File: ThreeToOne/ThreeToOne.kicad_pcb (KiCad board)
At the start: 2 copper layers, 216 parts, among them SW1 Switch, SW10 Switch, SW100 Switch, SW101 Switch, SW11 Switch, SW12 Switch, SW13 Switch, SW14 Switch, SW15 Switch, SW16 Switch, SW17 REsw, SW18 Switch, SW19 Switch, SW2 Switch, SW20 Switch, SW21 Switch, SW22 Switch, SW23 Switch, SW24 Switch, SW25 Switch, SW26 Switch, SW27 Switch, SW28 Switch, SW29 Switch, SW3 Switch, SW30 Switch, SW31 Switch, SW32 Switch, SW33 Switch, SW34 Switch, SW35 Switch, SW36 Switch, SW37 Switch, SW38 Switch, SW39 Switch, SW4 Switch, SW40 Switch, SW41 Switch, SW42 Switch, SW43 Switch, SW44 Switch, SW45 Switch, SW46 Switch, SW47 Switch, SW48 Switch, SW49 Switch, SW5 Switch, SW50 Switch, SW51 Switch, SW52 Switch, SW53 Switch, SW54 Switch, SW55 Switch, SW56 Switch, SW57 Switch, SW58 Switch, SW59 Switch, SW6 Switch, SW60 Switch, SW61 Switch, SW62 Switch, SW63 Switch, SW64 Switch, SW65 Switch, SW66 Switch, SW67 Switch, SW68 Switch, SW69 Switch, SW7 Switch, SW70 Switch, SW71 Switch, SW72 Switch, SW73 Switch, SW74 Switch, SW75 Switch, SW76 Switch, SW77 Switch, SW78 Switch, SW79 Switch, SW8 Switch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

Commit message: Laid out and routed rows/cols
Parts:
- removed H1, H10, H11, H12, H2, H3, H4, H5, H6, H7, H8, H9: Hole, KeyboardFootprints:Hole_2mm
- moved U2 457.7 mm to (464.3, 131.8)
- moved U1 81.4 mm to (302.4, 131.8)
- moved D75 18.7 mm to (303.2, 231.0)
- moved D52 0.79 mm to (521.5, 197.6)
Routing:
- net Row5: track 0.00 -> 331.6 mm
- net Col8: track 0.00 -> 180.6 mm
- net Col0: track 0.00 -> 180.3 mm
- net Col4: track 0.00 -> 179.6 mm
- net Row4: track 0.00 -> 176.8 mm
- net Col2: track 0.00 -> 175.2 mm
- net Row0: track 0.00 -> 174.6 mm
- net Row3: track 0.00 -> 174.6 mm
- net Row1: track 0.00 -> 174.6 mm
- net Row7: track 0.00 -> 174.6 mm
- net Row2: track 0.00 -> 174.6 mm
- net Col1: track 0.00 -> 174.6 mm
- net Col7: track 0.00 -> 173.0 mm
- net Col9: track 0.00 -> 171.7 mm
- net Col10: track 0.00 -> 171.6 mm
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
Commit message: Wired all of left half and some of right
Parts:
- added H1: Hole, KeyboardFootprints:Hole_2mm, F.Cu at (231.9, 75.5)
- added H10: Hole, KeyboardFootprints:Hole_2mm, F.Cu at (237.9, 81.5)
- added H11: Hole, KeyboardFootprints:Hole_2mm, F.Cu at (240.9, 78.5)
- added H12: Hole, KeyboardFootprints:Hole_2mm, F.Cu at (243.9, 75.5)
- added H2: Hole, KeyboardFootprints:Hole_2mm, F.Cu at (231.9, 78.5)
- added H3: Hole, KeyboardFootprints:Hole_2mm, F.Cu at (234.9, 75.5)
- added H4: Hole, KeyboardFootprints:Hole_2mm, F.Cu at (231.9, 81.5)
- added H5: Hole, KeyboardFootprints:Hole_2mm, F.Cu at (234.9, 78.5)
- added H6: Hole, KeyboardFootprints:Hole_2mm, F.Cu at (237.9, 75.5)
- added H7: Hole, KeyboardFootprints:Hole_2mm, F.Cu at (234.9, 81.5)
- added H8: Hole, KeyboardFootprints:Hole_2mm, F.Cu at (237.9, 78.5)
- added H9: Hole, KeyboardFootprints:Hole_2mm, F.Cu at (240.9, 75.5)
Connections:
- SW17 pad A: (no net) -> E3
- SW17 pad B: (no net) -> E4
- SW17 pad C: (no net) -> E2GND
- SW91 pad A: (no net) -> E1
- SW91 pad B: (no net) -> E2
- SW91 pad C: (no net) -> EGND1
- U1 pad 1: (no net) -> Col8
- U1 pad 10: (no net) -> Col4
- U1 pad 11: (no net) -> Col3
- U1 pad 12: (no net) -> Col2
- U1 pad 13: (no net) -> Row5
- U1 pad 14: (no net) -> Row4
- U1 pad 15: (no net) -> Row3
- U1 pad 16: (no net) -> Row2
- U1 pad 17: (no net) -> Row1
- U1 pad 18: (no net) -> Row0
- U1 pad 19: (no net) -> Col0
- U1 pad 2: (no net) -> Col7
- U1 pad 20: (no net) -> Col1
- U1 pad 21: (no net) -> TRRSVcc
- U1 pad 23: (no net) -> EGND1
- U1 pad 4: (no net) -> TRRSGnd
- U1 pad 5: (no net) -> Col6
- U1 pad 7: (no net) -> E2
- U1 pad 8: (no net) -> E1
- U1 pad 9: (no net) -> Col5
- U2 pad 1: (no net) -> Col9
- U2 pad 10: (no net) -> Col15
- U2 pad 11: (no net) -> Col16
- U2 pad 12: (no net) -> Col17
- U2 pad 13: (no net) -> E3
- U2 pad 14: (no net) -> E4
- U2 pad 15: (no net) -> Row11
- U2 pad 16: (no net) -> Row10
- U2 pad 17: (no net) -> Row9
- U2 pad 18: (no net) -> Row8
- U2 pad 19: (no net) -> Row7
- U2 pad 2: (no net) -> Col10
- U2 pad 20: (no net) -> Row6
- U2 pad 21: TRRSComm -> TRRSVcc
- U2 pad 23: (no net) -> E2GND
- U2 pad 3: TRRSComm -> (no net)
- U2 pad 4: (no net) -> TRRSGnd
- U2 pad 5: (no net) -> Col11
- U2 pad 7: (no net) -> Col12
- U2 pad 8: (no net) -> Col13
- U2 pad 9: (no net) -> Col14
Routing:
- net TRRSVcc: track 0.00 -> 162.6 mm, vias 0 -> 1
- net Row4: track 176.8 -> 339.0 mm, vias 0 -> 1
- net TRRSComm: track 0.00 -> 151.8 mm
- net Row3: track 174.6 -> 319.9 mm, vias 0 -> 1
- net E2: track 0.00 -> 144.3 mm, vias 0 -> 1
- net TRRSGnd: track 0.00 -> 140.5 mm
- net E1: track 0.00 -> 136.6 mm, vias 0 -> 1
- net Row2: track 174.6 -> 303.6 mm, vias 0 -> 1
- net EGND1: track 0.00 -> 115.6 mm, vias 0 -> 4
- net Row1: track 174.6 -> 286.6 mm, vias 0 -> 1
- net Row0: track 174.6 -> 269.3 mm, vias 0 -> 1
- net Col0: track 180.3 -> 273.5 mm
- net Col2: track 175.2 -> 266.9 mm
- net Col1: track 174.6 -> 252.5 mm
- net Col3: track 141.9 -> 217.9 mm
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
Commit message: Finished + gerbers
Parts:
- removed H1, H10, H11, H12, H2, H3, H4, H5, H6, H7, H8, H9: Hole, KeyboardFootprints:Hole_2mm
- added LED0: Diode, KeyboardFootprints:Diode, F.Cu at (461.2, 151.0)
- added LED1: Diode, KeyboardFootprints:Diode, F.Cu at (467.5, 150.8)
- added R0: Resistor, KeyboardFootprints:Resistor, F.Cu at (458.0, 151.0)
- added R1: Resistor, KeyboardFootprints:Resistor, F.Cu at (470.7, 150.8)
- U2: value ProMicro -> Elite-C; footprint KeyboardFootprints:ProMicro -> Keebio-Parts:Elite-C
- moved D89 18.3 mm to (264.3, 249.9)
- moved D87 17.5 mm to (225.4, 250.0)
- moved D88 17.5 mm to (244.5, 250.0)
- moved U1 9.52 mm to (292.9, 131.8)
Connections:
- U2 pad 13: E3 -> Net-(LED1-Pad1)
- U2 pad 14: E4 -> Net-(LED0-Pad1)
- U2 pad 15: Row11 -> Row8
- U2 pad 16: Row10 -> Row9
- U2 pad 17: Row9 -> Row10
- U2 pad 18: Row8 -> Row11
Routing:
- net Row11: track 160.9 -> 317.5 mm, vias 0 -> 1
- net E2GND: track 0.00 -> 147.8 mm, vias 0 -> 1
- net Row10: track 150.9 -> 295.7 mm, vias 0 -> 1
- net Row9: track 166.6 -> 294.4 mm, vias 0 -> 1
- net E4: track 0.00 -> 84.9 mm
- net E3: track 0.00 -> 76.8 mm, vias 0 -> 1
- net Row7: track 174.6 -> 247.4 mm, vias 0 -> 2
- net Row6: track 167.1 -> 223.8 mm
- net Net-(LED0-Pad1): track 0.00 -> 32.9 mm, vias 0 -> 1
- net Net-(LED1-Pad1): track 0.00 -> 29.5 mm, vias 0 -> 1
- net TRRSGnd: track 140.5 -> 168.8 mm, vias 0 -> 2
- net Row5: track 333.3 -> 306.0 mm
- net Row8: track 202.8 -> 229.0 mm, vias 0 -> 1
- net TRRSComm: track 151.8 -> 177.9 mm, vias 0 -> 2
- net Col13: track 165.1 -> 179.7 mm, vias 0 -> 2
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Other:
- board outline added: 343 x 133 mm

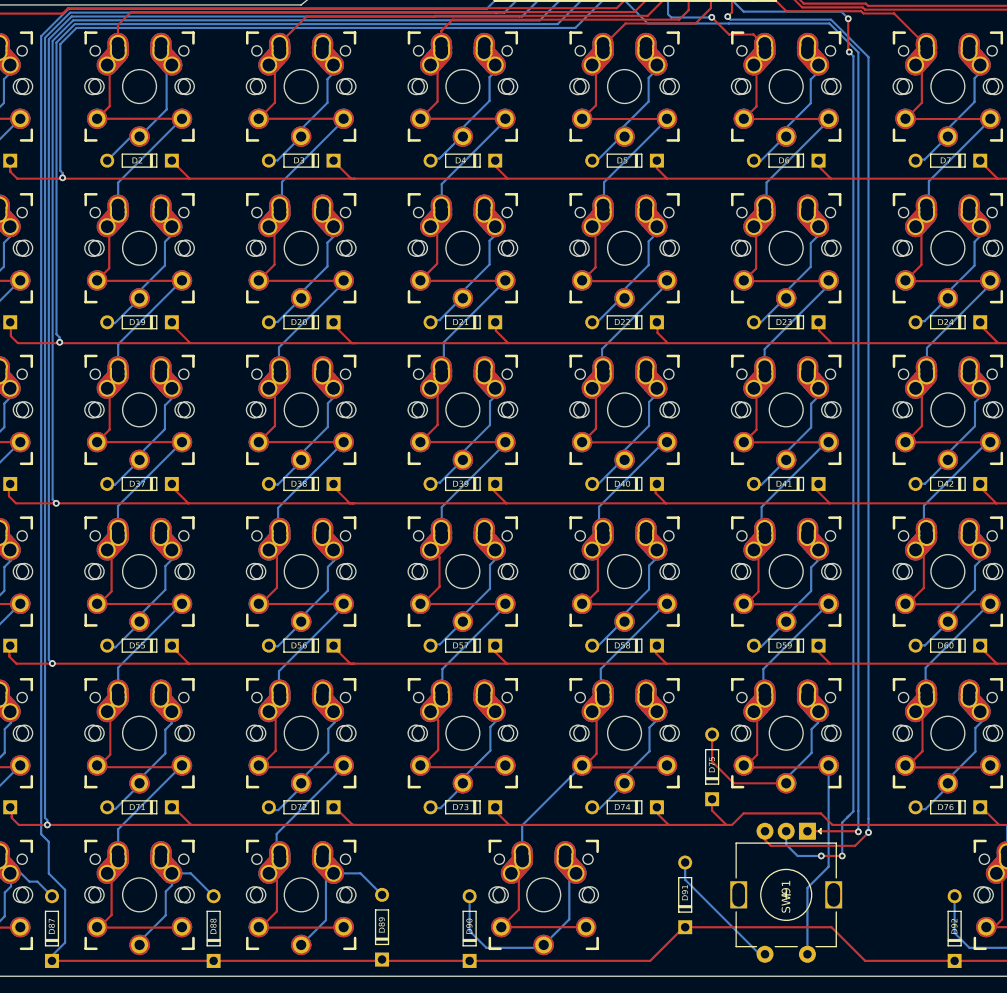
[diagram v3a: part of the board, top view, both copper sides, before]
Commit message: moved enc to the left
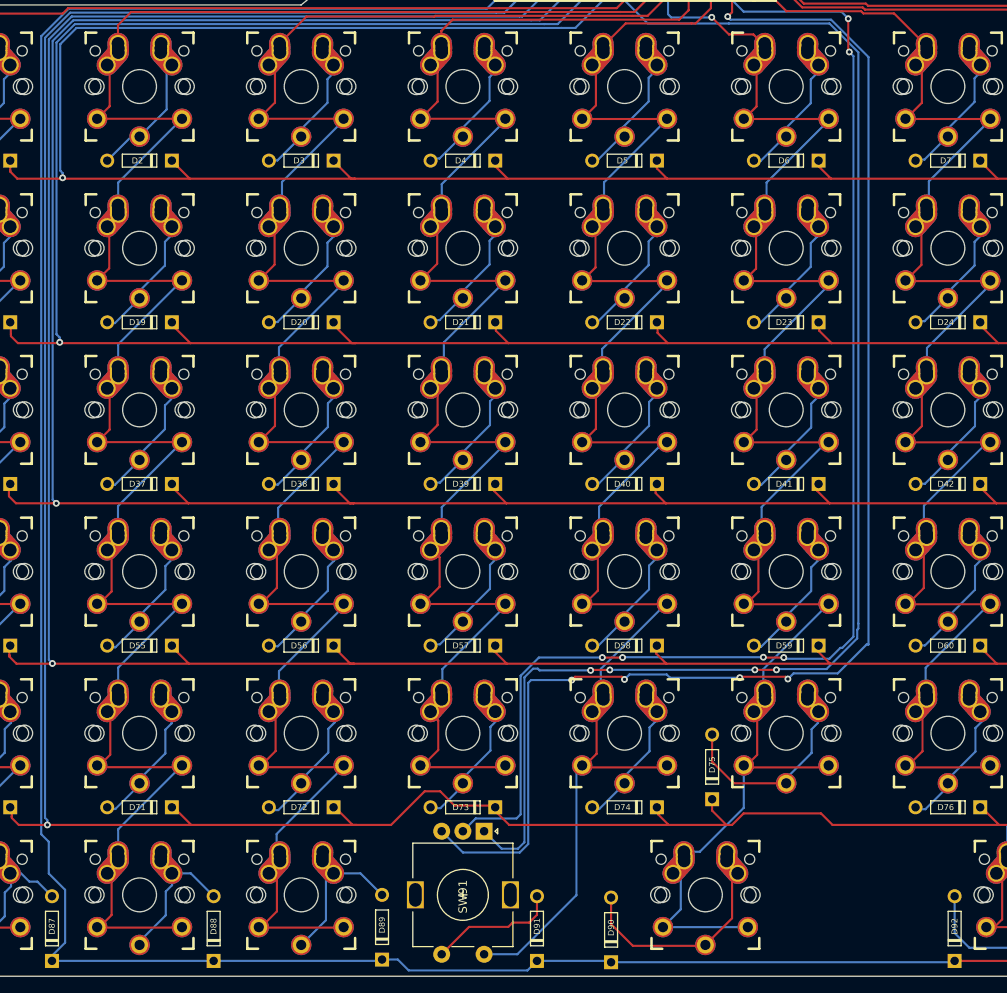
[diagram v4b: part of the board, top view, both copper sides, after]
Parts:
- moved SW91 38.1 mm to (273.8, 246.1)
- moved SW90 19.1 mm to (302.4, 246.1)
- moved D91 17.9 mm to (282.6, 250.0)
- moved D90 16.7 mm to (291.3, 250.2)
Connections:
- SW90 pad 1: Col4 -> Col5
- SW91 pad S2: Col5 -> Col4
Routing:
- net E1: track 147.2 -> 185.1 mm, vias 2 -> 5
- net E2: track 153.4 -> 190.4 mm, vias 2 -> 5
- net EGND1: track 125.0 -> 154.7 mm, vias 4 -> 6
- net Col5: track 202.6 -> 211.6 mm
- net Row5: track 306.0 -> 303.9 mm
- net Col4: track 228.7 -> 226.9 mm
- net Net-(D90-Pad1): track 23.8 -> 25.4 mm
- net Row4: track 329.2 -> 330.0 mm

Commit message: Finalization
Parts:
- moved SW91 38.1 mm to (311.9, 246.1)
- moved D91 19.8 mm to (302.4, 250.0)
- moved SW90 19.1 mm to (283.4, 246.1)
- moved D90 17.5 mm to (273.8, 250.0)
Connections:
- SW90 pad 1: Col5 -> Col3
- SW91 pad S2: Col4 -> Col5
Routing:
- net E2: track 190.4 -> 131.7 mm, vias 5 -> 2
- net E1: track 185.1 -> 137.3 mm, vias 5 -> 2
- net EGND1: track 154.7 -> 111.6 mm, vias 6 -> 0
- net Col3: track 207.4 -> 236.1 mm
- net Col4: track 226.9 -> 198.5 mm
- net Col5: track 211.6 -> 204.2 mm, vias 1 -> 2
- net Net-(D91-Pad1): track 15.3 -> 9.86 mm
